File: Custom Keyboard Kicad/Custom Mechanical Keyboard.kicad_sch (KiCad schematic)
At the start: 287 parts, among them J1 USB_C_Receptacle_USB2.0_16P, J2 Conn_01x04, J3 Conn_01x05, J4 Conn_01x06, J5 Conn_01x07, SW1 SW_SPST, SW10 SW_SPST, SW11 SW_SPST, SW12 SW_SPST, SW13 SW_SPST, SW14 SW_SPST, SW15 SW_SPST, SW16 SW_SPST, SW17 SW_SPST, SW18 SW_SPST, SW19 SW_SPST, SW2 SW_SPST, SW20 SW_SPST, SW21 SW_SPST, SW22 SW_SPST, SW23 SW_SPST, SW24 SW_SPST, SW25 SW_SPST, SW26 SW_SPST, SW27 SW_SPST, SW28 SW_SPST, SW29 SW_SPST, SW3 SW_SPST, SW30 SW_SPST, SW31 SW_SPST, SW32 SW_SPST, SW33 SW_SPST, SW34 SW_SPST, SW35 SW_SPST, SW36 SW_SPST, SW37 SW_SPST, SW38 SW_SPST, SW39 SW_SPST, SW4 SW_SPST, SW40 SW_SPST, SW41 SW_SPST, SW42 SW_SPST, SW43 SW_SPST, SW44 SW_SPST, SW45 SW_SPST, SW46 SW_SPST, SW47 SW_SPST, SW48 SW_SPST, SW49 SW_SPST, SW5 SW_SPST, SW50 SW_SPST, SW51 SW_SPST, SW52 SW_SPST, SW53 SW_SPST, SW54 SW_SPST, SW55 SW_SPST, SW56 SW_SPST, SW57 SW_SPST, SW58 SW_SPST, SW59 SW_SPST, SW6 SW_SPST, SW60 SW_SPST, SW61 SW_SPST, SW62 SW_SPST, SW63 SW_SPST, SW64 SW_SPST, SW65 SW_SPST, SW66 SW_SPST, SW67 SW_SPST, SW68 SW_SPST, SW69 SW_SPST, SW7 SW_SPST, SW70 SW_SPST, SW71 SW_SPST, SW72 SW_SPST, SW73 SW_SPST, SW74 SW_SPST, SW75 SW_SPST, SW76 SW_SPST, SW77 SW_SPST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

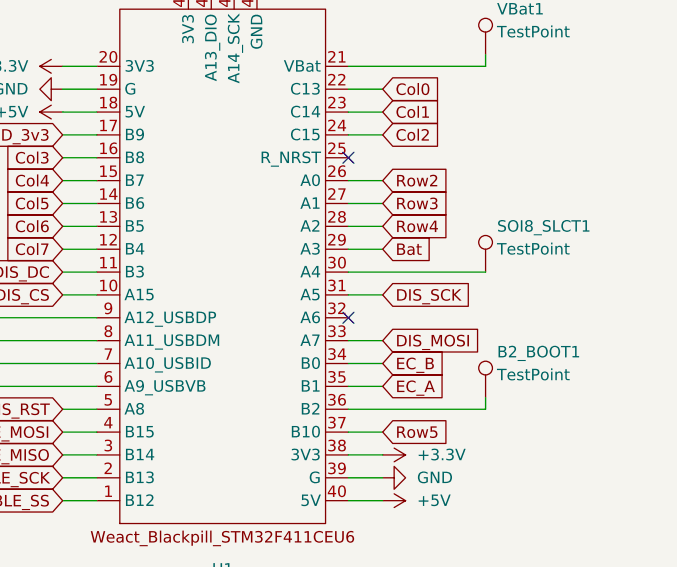
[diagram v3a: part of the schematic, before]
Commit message: Rewired rotary encoder, battery and row pins for space efficiency. Commit before export.
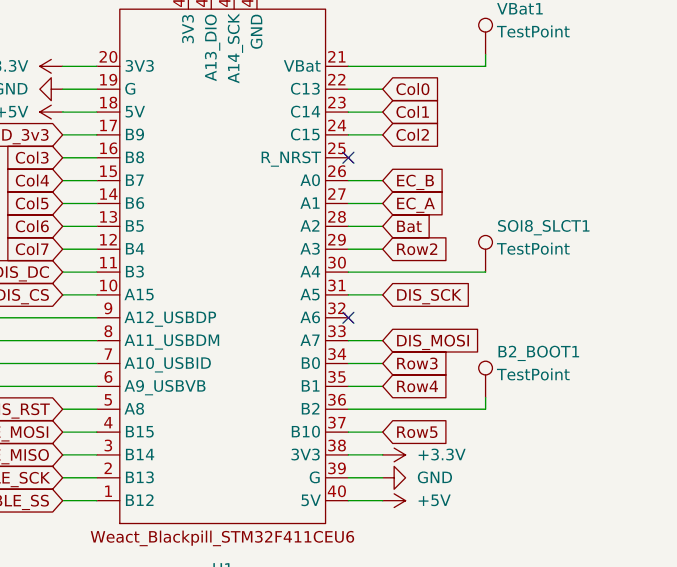
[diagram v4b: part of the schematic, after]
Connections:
- net Bat: now also U1.28 (A2); no longer U1.29 (A3)
- net EC_A: now also U1.27 (A1); no longer U1.35 (B1)
- net EC_B: now also U1.26 (A0); no longer U1.34 (B0)
- net Row2: now also U1.29 (A3); no longer U1.26 (A0)
- net Row3: now also U1.34 (B0); no longer U1.27 (A1)
- net Row4: now also U1.35 (B1); no longer U1.28 (A2)
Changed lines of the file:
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@@
 	(wire
 		(pts
-			(xy 539.75 186.69) (xy 535.94 186.69)
-		)
-		(stroke
-			(width 0)
-			(type default)
-		)
-	)
-	(wire
-		(pts
 			(xy 551.18 149.86) (xy 551.18 151.13)
 		)
@@
 	(wire
 		(pts
+			(xy 539.75 163.83) (xy 535.94 163.83)
+		)
+		(stroke
+			(width 0)
+			(type default)
+		)
+	)
+	(wire
+		(pts
 			(xy 69.85 185.42) (xy 69.85 187.96)
 		)
@@
 	(wire
 		(pts
+			(xy 539.75 186.69) (xy 535.94 186.69)
+		)
+		(stroke
+			(width 0)
+			(type default)
+		)
+	)
+	(wire
+		(pts
 			(xy 525.78 218.44) (xy 523.24 218.44)
 		)
@@
 	(wire
 		(pts
+			(xy 535.94 168.91) (xy 539.75 168.91)
+		)
+		(stroke
+			(width 0)
+			(type default)
+		)
+	)
+	(wire
+		(pts
 			(xy 135.89 88.9) (xy 137.16 88.9)
 		)
@@
 	(wire
 		(pts
-			(xy 539.75 163.83) (xy 535.94 163.83)
-		)
-		(stroke
-			(width 0)
-			(type default)
-		)
-	)
-	(wire
-		(pts
 			(xy 124.46 76.2) (xy 124.46 77.47)
 		)
@@
 	(wire
 		(pts
-			(xy 539.75 168.91) (xy 535.94 168.91)
-		)
-		(stroke
-			(width 0)
-			(type default)
-		)
-	)
-	(wire
-		(pts
 			(xy 287.02 54.61) (xy 287.02 55.88)
 		)
@@
 	(wire
 		(pts
-			(xy 539.75 166.37) (xy 535.94 166.37)
-		)
-		(stroke
-			(width 0)
-			(type default)
-		)
-	)
-	(wire
-		(pts
 			(xy 171.45 210.82) (xy 191.77 210.82)
 		)
@@
 	(wire
 		(pts
-			(xy 539.75 184.15) (xy 535.94 184.15)
-		)
-		(stroke
-			(width 0)
-			(type default)
-		)
-	)
-	(wire
-		(pts
 			(xy 313.69 231.14) (xy 313.69 228.6)
 		)
@@
 	(wire
 		(pts
+			(xy 539.75 166.37) (xy 535.94 166.37)
+		)
+		(stroke
+			(width 0)
+			(type default)
+		)
+	)
+	(wire
+		(pts
 			(xy 110.49 231.14) (xy 110.49 228.6)
 		)
@@
 	(wire
 		(pts
+			(xy 539.75 184.15) (xy 535.94 184.15)
+		)
+		(stroke
+			(width 0)
+			(type default)
+		)
+	)
+	(wire
+		(pts
 			(xy 287.02 45.72) (xy 288.29 45.72)
 		)
@@
 	(global_label "Row3"
 		(shape input)
-		(at 539.75 166.37 0)
+		(at 539.75 184.15 0)
 		(fields_autoplaced yes)
 		(effects
@@
 		)
 		(property "Intersheetrefs" "${INTERSHEET_REFS}"
-			(at 547.6942 166.37 0)
+			(at 547.6942 184.15 0)
 			(effects
 				(font
@@
 	(global_label "Row4"
 		(shape input)
-		(at 539.75 168.91 0)
+		(at 539.75 186.69 0)
 		(fields_autoplaced yes)
 		(effects
@@
 		)
 		(property "Intersheetrefs" "${INTERSHEET_REFS}"
-			(at 547.6942 168.91 0)
+			(at 547.6942 186.69 0)
 			(effects
 				(font
@@
 	(global_label "EC_B"
 		(shape input)
-		(at 539.75 184.15 0)
+		(at 539.75 163.83 0)
 		(fields_autoplaced yes)
 		(effects
@@
 		)
 		(property "Intersheetrefs" "${INTERSHEET_REFS}"
-			(at 547.3918 184.15 0)
+			(at 547.3918 163.83 0)
 			(effects
 				(font
@@
 	(global_label "EC_A"
 		(shape input)
-		(at 539.75 186.69 0)
+		(at 539.75 166.37 0)
 		(fields_autoplaced yes)
 		(effects
@@
 		)
 		(property "Intersheetrefs" "${INTERSHEET_REFS}"
-			(at 547.2104 186.69 0)
+			(at 547.2104 166.37 0)
 			(effects
 				(font
@@
 	(global_label "Bat"
 		(shape input)
-		(at 539.75 171.45 0)
+		(at 539.75 168.91 0)
 		(fields_autoplaced yes)
 		(effects
@@
 		)
 		(property "Intersheetrefs" "${INTERSHEET_REFS}"
-			(at 547.0289 171.45 0)
+			(at 547.0289 168.91 0)
 			(effects
 				(font
@@
 	(global_label "Row2"
 		(shape input)
-		(at 539.75 163.83 0)
+		(at 539.75 171.45 0)
 		(fields_autoplaced yes)
 		(effects
@@
 		)
 		(property "Intersheetrefs" "${INTERSHEET_REFS}"
-			(at 547.6942 163.83 0)
+			(at 547.6942 171.45 0)
 			(effects
 				(font

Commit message: Separated MCU and matrix boards, To be connected using FPC.
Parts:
- added J6, J7: Conn_01x20_Socket, PCM_marbastlib-various:XUNPU_FPC-05F-20PH20_1x20-1MP_P0.5mm_Horizontal, symbol Connector:Conn_01x20_Socket
- C1, C10, C11, C12, C2, C3, C4, C5, C6, C7, C8, C9: MFG Part # (none) -> GRM3195C2A104JA01D; Manufacturer (none) -> Murata Electronics; Type (none) -> SMD
- CAPS_LED1, LED1, LED10, LED11, LED12, LED13, LED14, LED15, LED16, LED17, LED18, LED19, LED2, LED20, LED21, LED22, LED23, LED24, LED25, LED26, LED27, LED28, LED29, LED3, LED30, LED31, LED32, LED33, LED34, LED35, LED36, LED37, LED38, LED39, LED4, LED40, LED41, LED42, LED43, LED44, LED45, LED46, LED47, LED48, LED49, LED5, LED50, LED51, LED52, LED53, LED54, LED55, LED56, LED57, LED58, LED59, LED6, LED60, LED61, LED62, LED63, LED64, LED65, LED66, LED67, LED68, LED69, LED7, LED70, LED71, LED72, LED73, LED74, LED75, LED76, LED77, LED78, LED79, LED8, LED80, LED81, LED82, LED83, LED84, LED9: MFG Part # (none) -> SK6803MINI-E; Manufacturer (none) -> Shenzhen Normand Electronic; Type (none) -> SMD
- D1, D10, D11, D12, D13, D14, D15, D16, D17, D18, D19, D2, D20, D21, D22, D23, D24, D25, D26, D27, D28, D29, D3, D30, D31, D32, D33, D34, D35, D36, D37, D38, D39, D4, D40, D41, D42, D43, D44, D45, D46, D47, D48, D49, D5, D50, D51, D52, D53, D54, D55, D56, D57, D58, D59, D6, D60, D61, D62, D63, D64, D65, D66, D67, D68, D69, D7, D70, D71, D72, D73, D74, D75, D76, D77, D78, D79, D8, D80, D81, D82, D83, D84, D9, ROT_D1: MFG Part # (none) -> 1N4148W-F; Manufacturer (none) -> Diodes Incorporated; Type (none) -> SMD
- J1: now not fitted
- J2: footprint Connector_JST:JST_PH_B4B-PH-K_1x04_P2.00mm_Vertical -> Connector_PinHeader_1.00mm:PinHeader_1x04_P1.00mm_Vertical; now not fitted
- J3: footprint Connector_JST:JST_PH_B5B-PH-K_1x05_P2.00mm_Vertical -> Connector_PinHeader_1.00mm:PinHeader_1x05_P1.00mm_Vertical
- J4: footprint Connector_JST:JST_PH_B6B-PH-K_1x06_P2.00mm_Vertical -> Connector_PinHeader_1.00mm:PinHeader_1x06_P1.00mm_Vertical
- J5: footprint Connector_JST:JST_PH_B7B-PH-K_1x07_P2.00mm_Vertical -> Connector_PinHeader_1.00mm:PinHeader_1x07_P1.00mm_Vertical
- R1, R2: MFG Part # (none) -> ERJ-8ENF5101V; Manufacturer (none) -> Panasonic; Type (none) -> SMD; now not fitted
- R3, R4: MFG Part # (none) -> ERJ-U08D1003V; Manufacturer (none) -> Panasonic; Type (none) -> SMD
- SW85: MFG Part # (none) -> JS202011AQN; Manufacturer (none) -> C&K; Type (none) -> Thru-Hole
- U2: MFG Part # (none) -> TXS0101DBV; Manufacturer (none) -> Texas Instruments; Type (none) -> SMD
- U3: MFG Part # (none) -> USBLC6-2SC6; Manufacturer (none) -> STMicroelectronics; Type (none) -> SMD
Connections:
- net +5V: now also J6.19 (Pin_19), J6.20 (Pin_20), J7.1 (Pin_1), J7.2 (Pin_2)
- net GND: now also J6.1 (Pin_1), J6.2 (Pin_2), J6.3 (Pin_3), J7.18 (Pin_18), J7.19 (Pin_19), J7.20 (Pin_20)
- net LED_5v: now also J7.3 (Pin_3); no longer U2.4 (B)
- net Col0 renamed C0
- net C0: now also J7.11 (Pin_11); no longer U1.22 (C13)
- net Col1 renamed C1
- net C1: now also J7.10 (Pin_10); no longer U1.23 (C14)
- net Col2 renamed C2
- net C2: now also J7.9 (Pin_9); no longer U1.24 (C15)
- net Col3 renamed C3
- net C3: now also J7.8 (Pin_8); no longer U1.16 (B8)
- net Col4 renamed C4
- net C4: now also J7.7 (Pin_7); no longer U1.15 (B7)
- net Col5 renamed C5
- net C5: now also J7.6 (Pin_6); no longer U1.14 (B6)
- net Col6 renamed C6
- net C6: now also J7.5 (Pin_5); no longer U1.13 (B5)
- net Col7 renamed C7
- net C7: now also J7.4 (Pin_4); no longer ROT_SW1.S1, U1.12 (B4)
- net Row0 renamed R0
- net R0: now also J7.12 (Pin_12); no longer U1.42 (A13_DIO)
- net Row1 renamed R1
- net R1: now also J7.13 (Pin_13); no longer ROT_D1.1 (K), U1.43 (A14_SCK)
- net Row2 renamed R2
- net R2: now also J7.14 (Pin_14); no longer U1.29 (A3)
- net Row3 renamed R3
- net R3: now also J7.15 (Pin_15); no longer U1.34 (B0)
- net Row4 renamed R4
- net R4: now also J7.16 (Pin_16); no longer U1.35 (B1)
- net Row5 renamed R5
- net R5: now also J7.17 (Pin_17); no longer U1.37 (B10)
- new net C0_IN: J6.10 (Pin_10), U1.22 (C13)
- new net C1_IN: J6.11 (Pin_11), U1.23 (C14)
- new net C2_IN: J6.12 (Pin_12), U1.24 (C15)
- new net C3_IN: J6.13 (Pin_13), U1.16 (B8)
- new net C4_IN: J6.14 (Pin_14), U1.15 (B7)
- new net C5_IN: J6.15 (Pin_15), U1.14 (B6)
- new net C6_IN: J6.16 (Pin_16), U1.13 (B5)
- new net C7_IN: J6.17 (Pin_17), ROT_SW1.S1, U1.12 (B4)
- new net LED_5v_OUT: J6.18 (Pin_18), U2.4 (B)
- new net R0_IN: J6.9 (Pin_9), U1.42 (A13_DIO)
- new net R1_IN: J6.8 (Pin_8), ROT_D1.1 (K), U1.43 (A14_SCK)
- new net R2_IN: J6.7 (Pin_7), U1.29 (A3)
- new net R3_IN: J6.6 (Pin_6), U1.34 (B0)
- new net R4_IN: J6.5 (Pin_5), U1.35 (B1)
- new net R5_IN: J6.4 (Pin_4), U1.37 (B10)
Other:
- moved on the sheet: A10_USB_ID1, A11_USB_DM1, A12_USB_DP1, A9_USB_VBUS1, B2_BOOT1, J4, J5, SOI8_SLCT1, U1, U2, VBat1

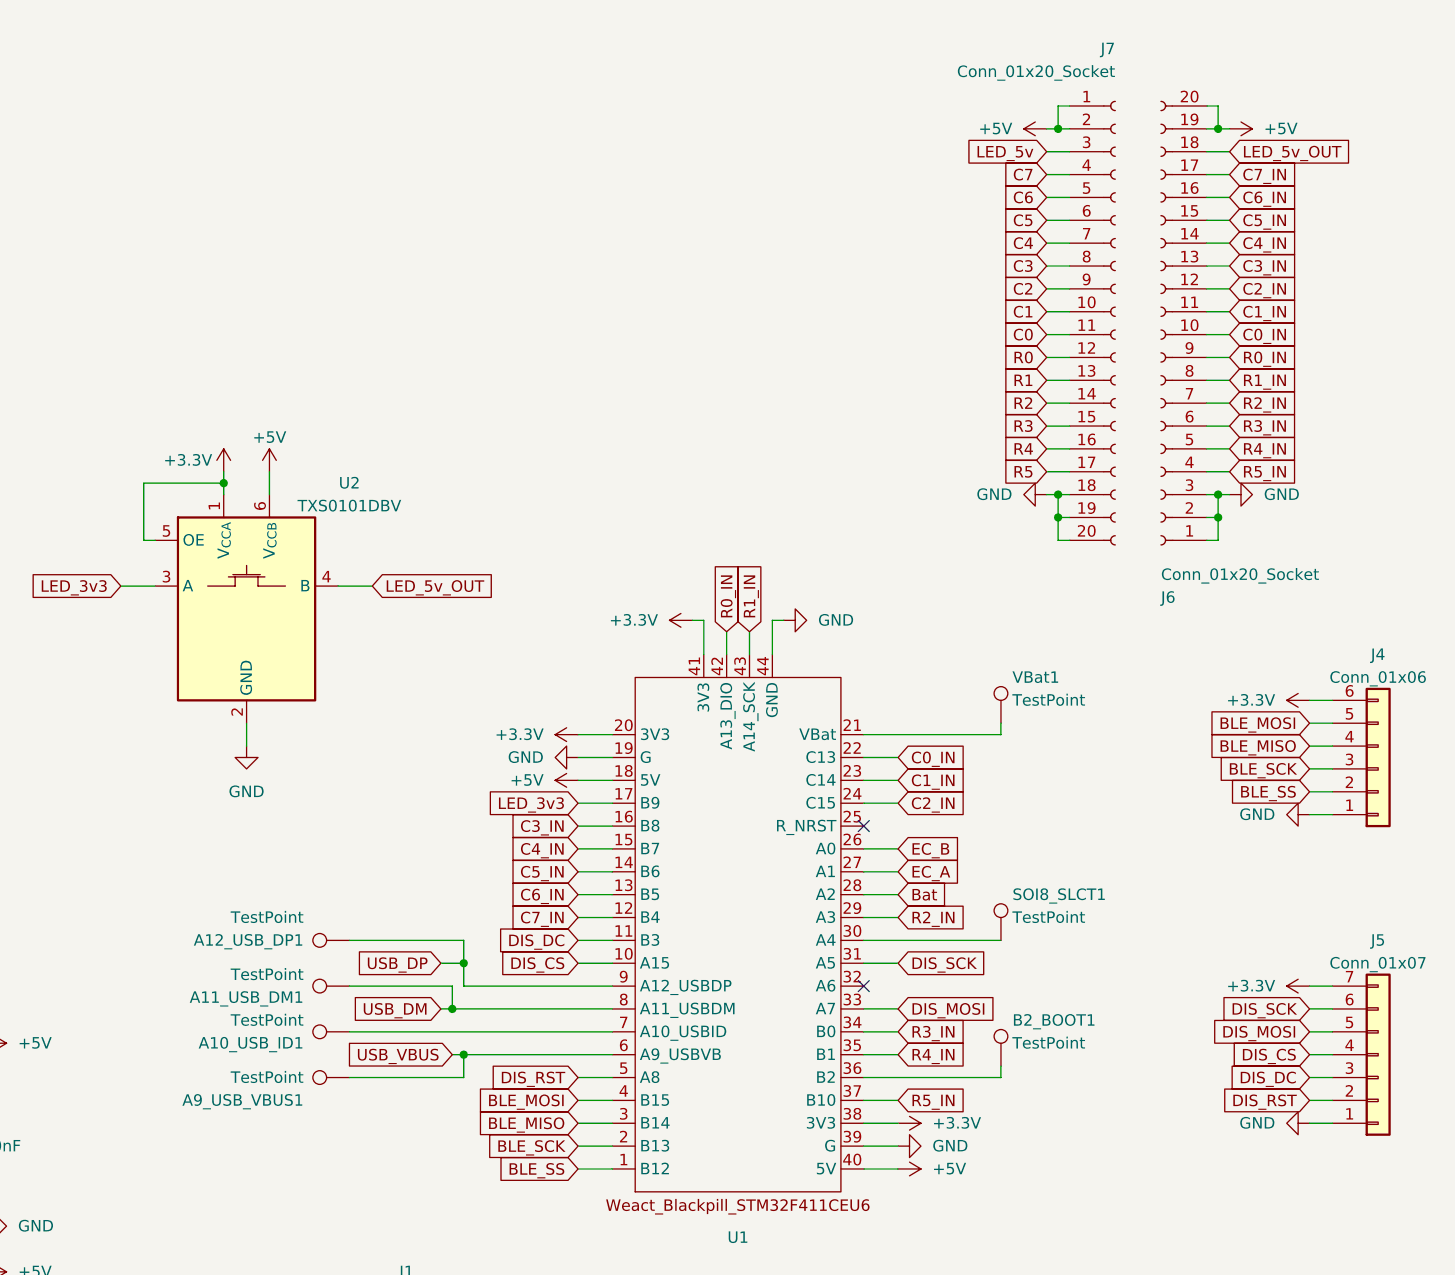
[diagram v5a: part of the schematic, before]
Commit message: Finished separate MCU and keyboard matrix boards, Added ribbon cable connectors and adjusted tracks to fit 0.05mm tolerance positioning. DRC checked, ready for export.
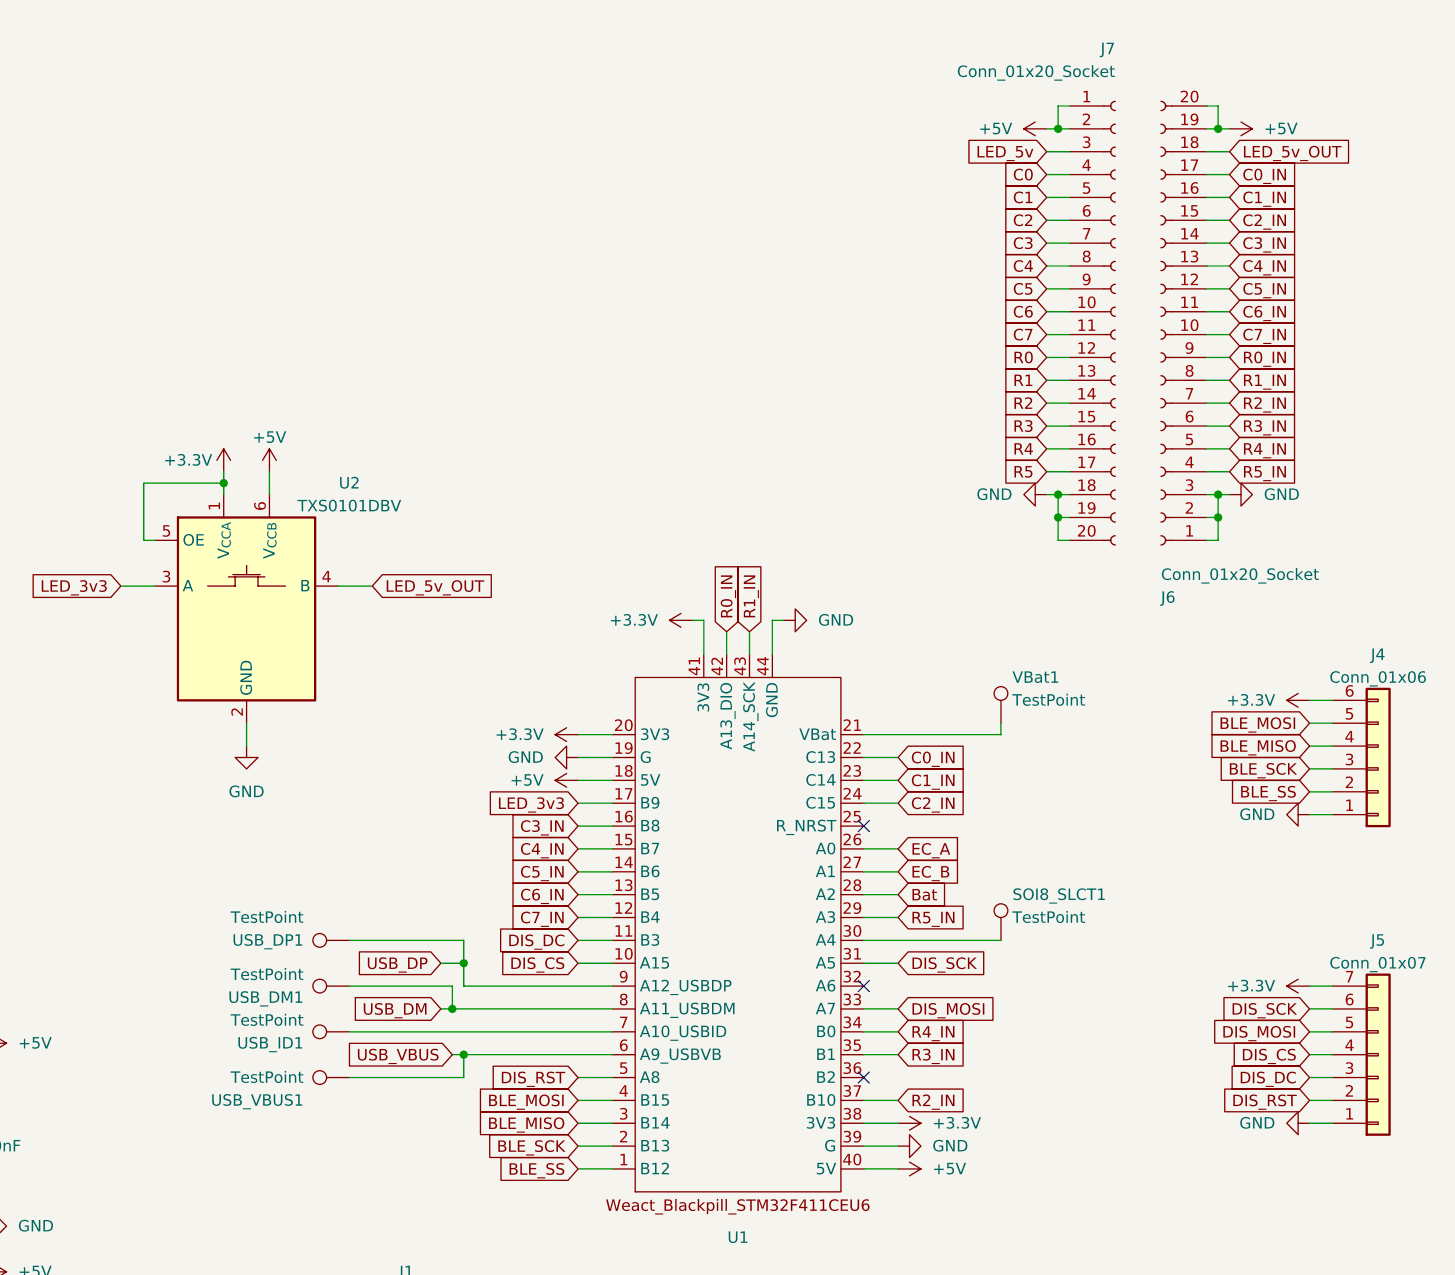
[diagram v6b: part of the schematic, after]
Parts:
- removed B2_BOOT1: TestPoint, TestPoint:TestPoint_Pad_D1.0mm, symbol Connector:TestPoint
- J2: footprint Connector_PinHeader_1.00mm:PinHeader_1x04_P1.00mm_Vertical -> Connector_PinHeader_2.00mm:PinHeader_1x04_P2.00mm_Vertical
- J3: footprint Connector_PinHeader_1.00mm:PinHeader_1x05_P1.00mm_Vertical -> Connector_PinHeader_2.00mm:PinHeader_1x05_P2.00mm_Vertical
- J4: footprint Connector_PinHeader_1.00mm:PinHeader_1x06_P1.00mm_Vertical -> Connector_PinHeader_2.00mm:PinHeader_1x06_P2.00mm_Vertical
- J5: footprint Connector_PinHeader_1.00mm:PinHeader_1x07_P1.00mm_Vertical -> Connector_PinHeader_2.00mm:PinHeader_1x07_P2.00mm_Vertical
- renumbered A11_USB_DM1 to USB_DM1, A12_USB_DP1 to USB_DP1, A10_USB_ID1 to USB_ID1, A9_USB_VBUS1 to USB_VBUS1
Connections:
- net C0: now also J7.4 (Pin_4); no longer J7.11 (Pin_11)
- net C0_IN: now also J6.17 (Pin_17); no longer J6.10 (Pin_10)
- net C1: now also J7.5 (Pin_5); no longer J7.10 (Pin_10)
- net C1_IN: now also J6.16 (Pin_16); no longer J6.11 (Pin_11)
- net C2: now also J7.6 (Pin_6); no longer J7.9 (Pin_9)
- net C2_IN: now also J6.15 (Pin_15); no longer J6.12 (Pin_12)
- net C3: now also J7.7 (Pin_7); no longer J7.8 (Pin_8)
- net C3_IN: now also J6.14 (Pin_14); no longer J6.13 (Pin_13)
- net C4: now also J7.8 (Pin_8); no longer J7.7 (Pin_7)
- net C4_IN: now also J6.13 (Pin_13); no longer J6.14 (Pin_14)
- net C5: now also J7.9 (Pin_9); no longer J7.6 (Pin_6)
- net C5_IN: now also J6.12 (Pin_12); no longer J6.15 (Pin_15)
- net C6: now also J7.10 (Pin_10); no longer J7.5 (Pin_5)
- net C6_IN: now also J6.11 (Pin_11); no longer J6.16 (Pin_16)
- net C7: now also J7.11 (Pin_11); no longer J7.4 (Pin_4)
- net C7_IN: now also J6.10 (Pin_10); no longer J6.17 (Pin_17)
- net EC_A: now also U1.26 (A0); no longer U1.27 (A1)
- net EC_B: now also U1.27 (A1); no longer U1.26 (A0)
- net R2_IN: now also U1.37 (B10); no longer U1.29 (A3)
- net R3_IN: now also U1.35 (B1); no longer U1.34 (B0)
- net R4_IN: now also U1.34 (B0); no longer U1.35 (B1)
- net R5_IN: now also U1.29 (A3); no longer U1.37 (B10)
- no-connect marks 5 -> 6
